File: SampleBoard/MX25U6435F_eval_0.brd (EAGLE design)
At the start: 29.2 x 42.9 mm, 12 parts, among them CN1 MX25U_IF_6PIN, U1 MIC5366-1.8YC5_, U6 MX25U6435F, U7 FXMA108_

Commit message: [WIP] デザイン修正
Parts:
- moved C42 22.9 mm to (7.62, 24.1), flipped to the bottom, turned to 90 degrees
- moved R25 19.9 mm to (2.54, 3.81), flipped to the bottom
- moved C45 15.5 mm to (6.35, 30.5), flipped to the bottom, turned to 270 degrees
- moved C46 12.8 mm to (6.35, 35.6), flipped to the bottom, turned to 90 degrees
- moved U7 10.9 mm to (7.62, 20.3)
- moved U6 10.2 mm to (7.62, 11.4)
- moved U1 9.16 mm to (7.62, 3.81), turned to 90 degrees
- moved C43 5.68 mm to (11.4, 3.81), flipped to the bottom, turned to 270 degrees
- moved C23 4.58 mm to (6.35, 3.81), flipped to the bottom, turned to 270 degrees
- moved R5 4.02 mm to (19.1, 33.0), flipped to the bottom
- moved C24 1.80 mm to (2.54, 24.1), flipped to the bottom
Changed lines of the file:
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@@
 <wire x1="29.19" y1="42.85" x2="0" y2="42.85" width="0" layer="20"/>
 <wire x1="0" y1="42.85" x2="0" y2="0" width="0" layer="20"/>
+<wire x1="0" y1="24.13" x2="12.7" y2="24.13" width="0.4064" layer="51"/>
+<wire x1="12.7" y1="24.13" x2="12.7" y2="0" width="0.4064" layer="51"/>
+<wire x1="12.7" y1="0" x2="0" y2="0" width="0.4064" layer="51"/>
+<wire x1="0" y1="0" x2="0" y2="24.13" width="0.4064" layer="51"/>
 </plain>
 <attributes>
@@
 </autorouter>
 <elements>
-<element name="C23" library="Parts" package="SMD_1608_DEV" value="1uF X5R" x="2.54" y="6.35"/>
-<element name="C24" library="Parts" package="C1210_TPST_DEV" value="10uF" x="3.81" y="25.4" rot="R90"/>
-<element name="C42" library="Parts" package="SMD_1608_DEV" value="0.1uF" x="26.67" y="36.83"/>
-<element name="C43" library="Parts" package="SMD_1608_DEV" value="1uF X5R" x="16.51" y="6.35"/>
-<element name="C45" library="Parts" package="SMD_1608_DEV" value="0.1uF" x="21.59" y="33.02"/>
-<element name="C46" library="Parts" package="SMD_1608_DEV" value="0.1uF" x="19.05" y="36.83"/>
+<element name="C23" library="Parts" package="SMD_1608_DEV" value="1uF X5R" x="6.35" y="3.81" rot="MR270"/>
+<element name="C24" library="Parts" package="C1210_TPST_DEV" value="10uF" x="2.54" y="24.13" rot="MR90"/>
+<element name="C42" library="Parts" package="SMD_1608_DEV" value="0.1uF" x="7.62" y="24.13" rot="MR90"/>
+<element name="C43" library="Parts" package="SMD_1608_DEV" value="1uF X5R" x="11.43" y="3.81" rot="MR270"/>
+<element name="C45" library="Parts" package="SMD_1608_DEV" value="0.1uF" x="6.35" y="30.48" rot="MR270"/>
+<element name="C46" library="Parts" package="SMD_1608_DEV" value="0.1uF" x="6.35" y="35.56" rot="MR90"/>
 <element name="CN1" library="PartsForProto" package="HEADER_6PIN" value="MX25U_IF_6PIN" x="24.13" y="27.94" rot="R270"/>
-<element name="R25" library="Parts" package="SMD_1608_DEV" value="0" x="20.32" y="12.7" rot="R90"/>
-<element name="R5" library="Parts" package="SMD_1608_DEV" value="10k" x="17.78" y="29.21" rot="R90"/>
-<element name="U1" library="Parts" package="SC-70-5_DEV" value="MIC5366-1.8YC5_" x="12.7" y="11.43"/>
-<element name="U6" library="Parts" package="SO8" value="MX25U6435F" x="12.7" y="20.32"/>
-<element name="U7" library="Parts" package="DQFN20_DEV" value="FXMA108_" x="11.43" y="30.48"/>
+<element name="R25" library="Parts" package="SMD_1608_DEV" value="0" x="2.54" y="3.81" rot="MR90"/>
+<element name="R5" library="Parts" package="SMD_1608_DEV" value="10k" x="19.05" y="33.02" rot="MR90"/>
+<element name="U1" library="Parts" package="SC-70-5_DEV" value="MIC5366-1.8YC5_" x="7.62" y="3.81" rot="R90"/>
+<element name="U6" library="Parts" package="SO8" value="MX25U6435F" x="7.62" y="11.43"/>
+<element name="U7" library="Parts" package="DQFN20_DEV" value="FXMA108_" x="7.62" y="20.32"/>
 </elements>
 <signals>
@@
 <contactref element="R25" pad="1"/>
 <contactref element="CN1" pad="1"/>
-<wire x1="20.32" y1="11.6" x2="24.13" y2="27.94" width="0" layer="19" extent="1-1"/>
+<wire x1="2.54" y1="2.71" x2="24.13" y2="27.94" width="0" layer="19" extent="16-16"/>
 </signal>
 <signal name="0V">
@@
 <vertex x="-1.27" y="-1.27"/>
 </polygon>
-<wire x1="22.69" y1="33.02" x2="27.77" y2="36.83" width="0" layer="19" extent="1-1"/>
-<wire x1="20.15" y1="36.83" x2="22.69" y2="33.02" width="0" layer="19" extent="1-1"/>
-<wire x1="17.78" y1="28.11" x2="22.69" y2="33.02" width="0" layer="19" extent="1-1"/>
-<wire x1="14.13" y1="30.23" x2="17.78" y2="28.11" width="0" layer="19" extent="1-1"/>
-<wire x1="3.81" y1="27.1" x2="14.13" y2="30.23" width="0" layer="19" extent="1-1"/>
-<wire x1="14.605" y1="17.72" x2="17.78" y2="28.11" width="0" layer="19" extent="1-1"/>
-<wire x1="12.7" y1="10.005" x2="14.605" y2="17.72" width="0" layer="19" extent="1-1"/>
-<wire x1="17.61" y1="6.35" x2="12.7" y2="10.005" width="0" layer="19" extent="1-1"/>
-<wire x1="3.64" y1="6.35" x2="12.7" y2="10.005" width="0" layer="19" extent="1-1"/>
-<wire x1="24.13" y1="15.24" x2="14.605" y2="17.72" width="0" layer="19" extent="1-1"/>
+<via x="17.78" y="11.43" extent="1-16" drill="0.6"/>
+<via x="16.51" y="20.32" extent="1-16" drill="0.6"/>
+<via x="16.51" y="30.48" extent="1-16" drill="0.6"/>
+<wire x1="16.51" y1="30.48" x2="10.32" y2="20.07" width="0" layer="19" extent="1-1"/>
+<wire x1="9.525" y1="8.83" x2="16.51" y2="20.32" width="0" layer="19" extent="1-1"/>
+<wire x1="9.045" y1="3.81" x2="6.35" y2="2.71" width="0" layer="19" extent="1-16"/>
 </signal>
 <signal name="!CS!">
 <contactref element="U6" pad="1"/>
 <contactref element="U7" pad="3"/>
-<wire x1="10.795" y1="17.72" x2="10.18" y2="28.78" width="0" layer="19" extent="1-1"/>
+<wire x1="5.715" y1="8.83" x2="6.37" y2="18.62" width="0" layer="19" extent="1-1"/>
 </signal>
 <signal name="SI">
 <contactref element="U6" pad="5"/>
 <contactref element="U7" pad="5"/>
-<wire x1="14.605" y1="22.92" x2="11.18" y2="28.78" width="0" layer="19" extent="1-1"/>
+<wire x1="9.525" y1="14.03" x2="7.37" y2="18.62" width="0" layer="19" extent="1-1"/>
 </signal>
 <signal name="SO">
 <contactref element="U6" pad="2"/>
 <contactref element="U7" pad="6"/>
-<wire x1="12.065" y1="17.72" x2="11.68" y2="28.78" width="0" layer="19" extent="1-1"/>
+<wire x1="6.985" y1="8.83" x2="7.87" y2="18.62" width="0" layer="19" extent="1-1"/>
 </signal>
 <signal name="SCLK">
 <contactref element="U6" pad="6"/>
 <contactref element="U7" pad="8"/>
-<wire x1="13.335" y1="22.92" x2="12.68" y2="28.78" width="0" layer="19" extent="1-1"/>
+<wire x1="8.255" y1="14.03" x2="8.87" y2="18.62" width="0" layer="19" extent="1-1"/>
 </signal>
 <signal name="VCC_MEM">
@@
 <contactref element="U7" pad="20"/>
 <contactref element="C46" pad="1"/>
-<wire x1="8.73" y1="30.73" x2="17.95" y2="36.83" width="0" layer="19" extent="1-1"/>
-<wire x1="20.32" y1="13.8" x2="8.73" y2="30.73" width="0" layer="19" extent="1-1"/>
-<wire x1="13.35" y1="10.005" x2="20.32" y2="13.8" width="0" layer="19" extent="1-1"/>
-<wire x1="12.05" y1="10.005" x2="13.35" y2="10.005" width="0" layer="19" extent="1-1"/>
-<wire x1="15.41" y1="6.35" x2="13.35" y2="10.005" width="0" layer="19" extent="1-1"/>
+<wire x1="6.35" y1="34.46" x2="4.92" y2="20.57" width="0" layer="19" extent="1-16"/>
+<wire x1="9.045" y1="4.46" x2="4.92" y2="20.57" width="0" layer="19" extent="1-1"/>
+<wire x1="9.045" y1="3.16" x2="9.045" y2="4.46" width="0" layer="19" extent="1-1"/>
+<wire x1="11.43" y1="4.91" x2="9.045" y2="3.16" width="0" layer="19" extent="1-16"/>
+<wire x1="2.54" y1="4.91" x2="9.045" y2="3.16" width="0" layer="19" extent="1-16"/>
 </signal>
 <signal name="!OE!">
 <contactref element="R5" pad="2"/>
 <contactref element="U7" pad="11"/>
-<wire x1="14.13" y1="30.73" x2="17.78" y2="30.31" width="0" layer="19" extent="1-1"/>
+<via x="16.51" y="35.56" extent="1-16" drill="0.6"/>
+<wire x1="16.51" y1="35.56" x2="19.05" y2="34.12" width="0" layer="19" extent="16-16"/>
+<wire x1="10.32" y1="20.57" x2="16.51" y2="35.56" width="0" layer="19" extent="1-1"/>
 </signal>
 <signal name="+1V8">
@@
 <contactref element="U7" pad="1"/>
 <contactref element="C45" pad="1"/>
-<wire x1="20.49" y1="33.02" x2="25.57" y2="36.83" width="0" layer="19" extent="1-1"/>
-<wire x1="8.73" y1="30.23" x2="20.49" y2="33.02" width="0" layer="19" extent="1-1"/>
-<wire x1="10.795" y1="22.92" x2="8.73" y2="30.23" width="0" layer="19" extent="1-1"/>
-<wire x1="12.065" y1="22.92" x2="10.795" y2="22.92" width="0" layer="19" extent="1-1"/>
-<wire x1="13.335" y1="17.72" x2="12.065" y2="22.92" width="0" layer="19" extent="1-1"/>
-<wire x1="12.05" y1="12.855" x2="13.335" y2="17.72" width="0" layer="19" extent="1-1"/>
-<wire x1="3.81" y1="23.7" x2="10.795" y2="22.92" width="0" layer="19" extent="1-1"/>
-<wire x1="1.44" y1="6.35" x2="12.05" y2="12.855" width="0" layer="19" extent="1-1"/>
+<wire x1="6.35" y1="31.58" x2="4.92" y2="20.07" width="0" layer="19" extent="1-16"/>
+<wire x1="7.62" y1="23.03" x2="6.35" y2="31.58" width="0" layer="19" extent="16-16"/>
+<wire x1="5.715" y1="14.03" x2="7.62" y2="23.03" width="0" layer="19" extent="1-16"/>
+<wire x1="6.985" y1="14.03" x2="5.715" y2="14.03" width="0" layer="19" extent="1-1"/>
+<wire x1="2.54" y1="22.43" x2="7.62" y2="23.03" width="0" layer="19" extent="16-16"/>
+<wire x1="8.255" y1="8.83" x2="6.985" y2="14.03" width="0" layer="19" extent="1-1"/>
+<wire x1="6.35" y1="4.91" x2="8.255" y2="8.83" width="0" layer="19" extent="1-16"/>
+<wire x1="6.195" y1="3.16" x2="6.35" y2="4.91" width="0" layer="19" extent="1-16"/>
 </signal>
 <signal name="PA15">
 <contactref element="U7" pad="18"/>
 <contactref element="CN1" pad="2"/>
-<wire x1="10.18" y1="32.18" x2="24.13" y2="25.4" width="0" layer="19" extent="1-1"/>
+<wire x1="6.37" y1="22.02" x2="24.13" y2="25.4" width="0" layer="19" extent="1-1"/>
 </signal>
 <signal name="PC12">
 <contactref element="U7" pad="16"/>
 <contactref element="CN1" pad="3"/>
-<wire x1="11.18" y1="32.18" x2="24.13" y2="22.86" width="0" layer="19" extent="1-1"/>
+<wire x1="7.37" y1="22.02" x2="24.13" y2="22.86" width="0" layer="19" extent="1-1"/>
 </signal>
 <signal name="PC11">
 <contactref element="U7" pad="15"/>
 <contactref element="CN1" pad="4"/>
-<wire x1="11.68" y1="32.18" x2="24.13" y2="20.32" width="0" layer="19" extent="1-1"/>
+<wire x1="24.13" y1="20.32" x2="7.87" y2="22.02" width="0" layer="19" extent="1-1"/>
 </signal>
 <signal name="PC10">
 <contactref element="U7" pad="13"/>
 <contactref element="CN1" pad="5"/>
-<wire x1="24.13" y1="17.78" x2="12.68" y2="32.18" width="0" layer="19" extent="1-1"/>
+<wire x1="24.13" y1="17.78" x2="8.87" y2="22.02" width="0" layer="19" extent="1-1"/>
 </signal>
 </signals>

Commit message: 配線を全面的に修正
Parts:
- moved CN1 22.9 mm to (16.5, 6.35), turned to 90 degrees
- moved C24 16.7 mm to (7.62, 8.26), turned to 180 degrees
- moved C45 16.6 mm to (5.08, 14.0), turned to 180 degrees
- moved R5 13.5 mm to (10.2, 22.9), turned to 180 degrees
- moved R25 13.0 mm to (15.2, 1.27), turned to 0 degrees
- moved C46 12.8 mm to (5.08, 22.9), turned to 180 degrees
- moved C42 6.84 mm to (5.08, 17.8), turned to 180 degrees
- moved C23 4.46 mm to (1.91, 3.49), turned to 90 degrees
- moved C43 3.88 mm to (8.26, 1.59), turned to 0 degrees
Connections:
- net PC10: now also U7.16; no longer U7.13
- net PC11: now also U7.14; no longer U7.15
- net PC12: now also U7.12; no longer U7.16
- net SCLK: now also U7.5; no longer U7.8
- net SI: now also U7.9; no longer U7.5
- net SO: now also U7.7; no longer U7.6
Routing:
- net VCC_MEM: track 0.00 -> 52.0 mm, vias 0 -> 3
- net +1V8: track 0.00 -> 45.3 mm, vias 0 -> 4
- net PA15: track 0.00 -> 28.3 mm
- net PC12: track 0.00 -> 18.3 mm
- net PC11: track 0.00 -> 17.9 mm
- net PC10: track 0.00 -> 17.5 mm
- net !CS!: track 0.00 -> 11.1 mm
- net SO: track 0.00 -> 10.8 mm
- net 0V: track 0.00 -> 8.37 mm
- net +3V3: track 0.00 -> 5.15 mm
- net SCLK: track 0.00 -> 4.96 mm
- net SI: track 0.00 -> 4.65 mm
- net !OE!: track 0.00 -> 4.14 mm
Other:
- board size 29.2 x 42.9 mm -> 19.1 x 25.4 mm

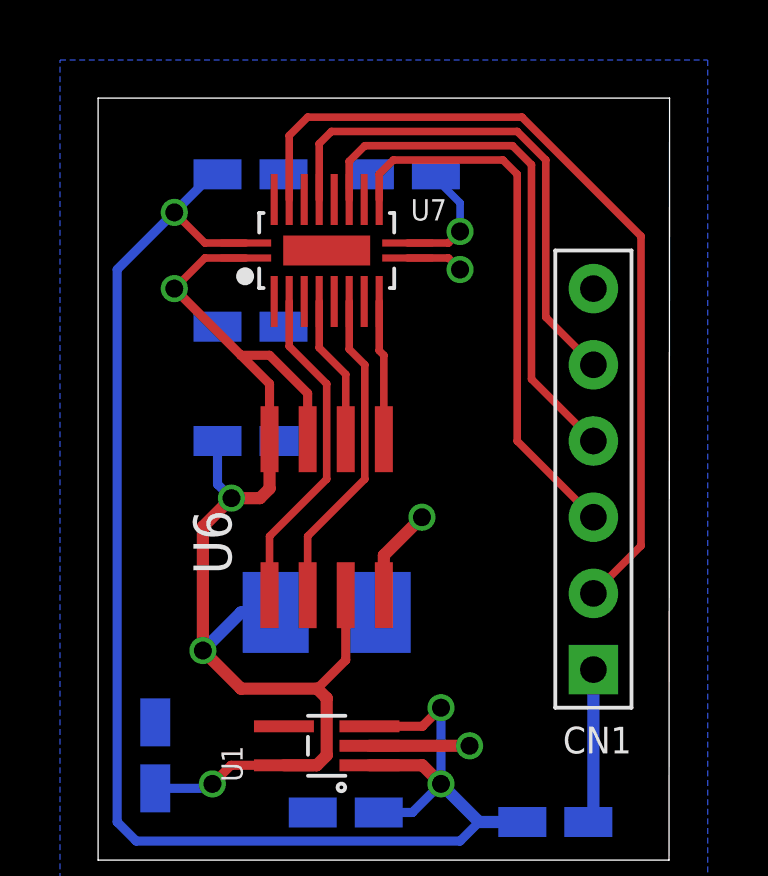
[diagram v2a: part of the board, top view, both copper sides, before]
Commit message: 評価回路を修正
・配線を小修正
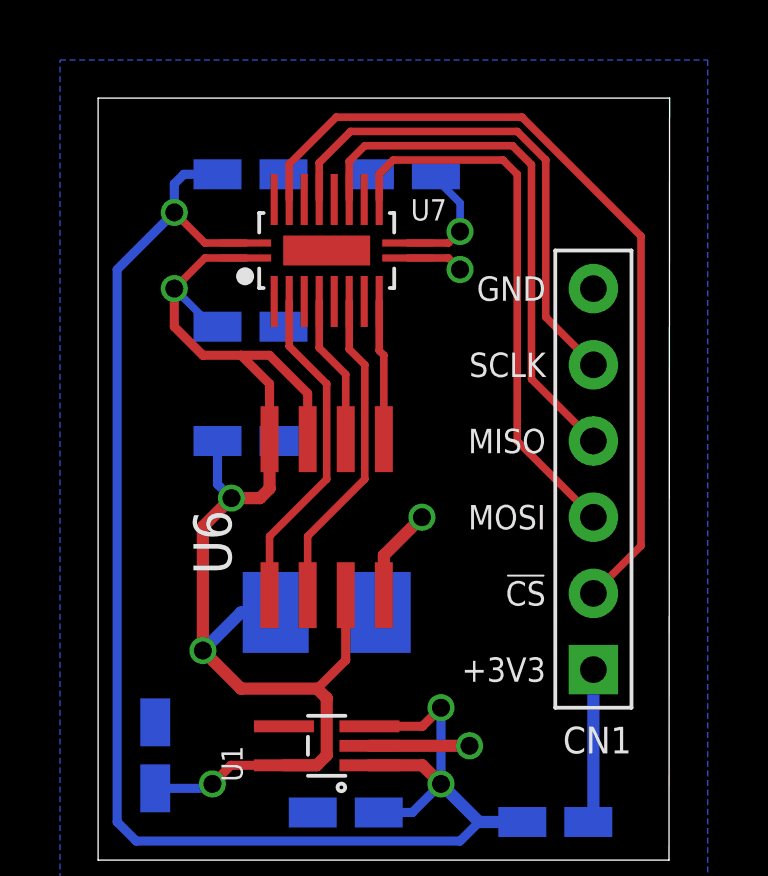
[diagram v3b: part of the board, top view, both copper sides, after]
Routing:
- net +1V8: track 45.3 -> 46.1 mm
- net VCC_MEM: track 52.0 -> 52.6 mm
- net PA15: track 28.3 -> 27.8 mm
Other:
- board text added: "!CS!"
- board text added: "+3V3"
- board text added: "GND"
- board text added: "MISO"
- board text added: "MOSI"
- board text added: "SCLK"
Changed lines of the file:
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@@
 <setting verticaltext="up"/>
 </settings>
-<grid distance="0.05" unitdist="inch" unit="mil" style="lines" multiple="1" display="yes" altdistance="0.025" altunitdist="inch" altunit="inch"/>
+<grid distance="12.5" unitdist="mil" unit="mil" style="lines" multiple="1" display="yes" altdistance="0.025" altunitdist="inch" altunit="inch"/>
 <layers>
 <layer number="1" name="Top" color="4" fill="1" visible="yes" active="yes"/>
@@
 <wire x1="19.05" y1="25.4" x2="0" y2="25.4" width="0" layer="20"/>
 <wire x1="0" y1="25.4" x2="0" y2="0" width="0" layer="20"/>
+<text x="14.9225" y="19.05" size="0.8128" layer="21" align="center-right">GND</text>
+<text x="14.9225" y="16.51" size="0.8128" layer="21" align="center-right">SCLK</text>
+<text x="14.9225" y="13.97" size="0.8128" layer="21" align="center-right">MISO</text>
+<text x="14.9225" y="11.43" size="0.8128" layer="21" align="center-right">MOSI</text>
+<text x="14.9225" y="8.89" size="0.8128" layer="21" align="center-right">!CS!</text>
+<text x="14.9225" y="6.35" size="0.8128" layer="21" align="center-right">+3V3</text>
 </plain>
 <attributes>
@@
 <wire x1="4.92" y1="20.57" x2="3.56" y2="20.57" width="0.254" layer="1"/>
 <wire x1="3.56" y1="20.57" x2="2.54" y2="21.59" width="0.254" layer="1"/>
-<wire x1="2.54" y1="21.59" x2="3.81" y2="22.86" width="0.3048" layer="16"/>
-<wire x1="3.81" y1="22.86" x2="3.98" y2="22.86" width="0.3048" layer="16"/>
 <wire x1="12.7" y1="1.27" x2="12.065" y2="0.635" width="0.3048" layer="16"/>
 <wire x1="12.065" y1="0.635" x2="1.27" y2="0.635" width="0.3048" layer="16"/>
@@
 <wire x1="11.43" y1="2.54" x2="12.7" y2="1.27" width="0.4064" layer="16"/>
 <wire x1="14.14" y1="1.27" x2="12.7" y2="1.27" width="0.4064" layer="16"/>
+<wire x1="3.98" y1="22.86" x2="2.8575" y2="22.86" width="0.3048" layer="16"/>
+<wire x1="2.8575" y1="22.86" x2="2.54" y2="22.5425" width="0.3048" layer="16"/>
+<wire x1="2.54" y1="22.5425" x2="2.54" y2="21.59" width="0.3048" layer="16"/>
 </signal>
 <signal name="!OE!">
@@
 <wire x1="5.715" y1="14.03" x2="5.715" y2="15.875" width="0.3048" layer="1"/>
 <wire x1="5.715" y1="15.875" x2="4.7625" y2="16.8275" width="0.3048" layer="1"/>
-<wire x1="4.7625" y1="16.8275" x2="2.54" y2="19.05" width="0.3048" layer="1"/>
 <wire x1="6.985" y1="14.03" x2="6.985" y2="15.5575" width="0.3048" layer="1"/>
 <wire x1="3.98" y1="13.97" x2="3.98" y2="12.53" width="0.3048" layer="16"/>
@@
 <wire x1="8.255" y1="8.83" x2="8.255" y2="6.6675" width="0.3048" layer="1"/>
 <wire x1="8.255" y1="6.6675" x2="7.3025" y2="5.715" width="0.3048" layer="1"/>
+<wire x1="4.7625" y1="16.8275" x2="3.4925" y2="16.8275" width="0.3048" layer="1"/>
+<wire x1="3.4925" y1="16.8275" x2="2.54" y2="17.78" width="0.3048" layer="1"/>
+<wire x1="2.54" y1="17.78" x2="2.54" y2="19.05" width="0.3048" layer="1"/>
 </signal>
 <signal name="PA15">
 <contactref element="U7" pad="18"/>
 <contactref element="CN1" pad="2"/>
-<wire x1="6.37" y1="22.02" x2="6.37" y2="24.15" width="0.254" layer="1"/>
-<wire x1="6.37" y1="24.15" x2="6.985" y2="24.765" width="0.254" layer="1"/>
 <wire x1="18.0975" y1="10.4775" x2="16.51" y2="8.89" width="0.254" layer="1"/>
-<wire x1="6.985" y1="24.765" x2="14.12875" y2="24.765" width="0.254" layer="1"/>
+<wire x1="7.9375" y1="24.765" x2="14.12875" y2="24.765" width="0.254" layer="1"/>
 <wire x1="14.12875" y1="24.765" x2="18.0975" y2="20.79625" width="0.254" layer="1"/>
 <wire x1="18.0975" y1="20.79625" x2="18.0975" y2="10.4775" width="0.254" layer="1"/>
+<wire x1="6.37" y1="22.02" x2="6.37" y2="23.1975" width="0.254" layer="1"/>
+<wire x1="6.37" y1="23.1975" x2="7.9375" y2="24.765" width="0.254" layer="1"/>
 </signal>
 <signal name="PC12">
@@
 <contactref element="CN1" pad="5"/>
 <contactref element="U7" pad="16"/>
-<wire x1="7.37" y1="22.02" x2="7.37" y2="23.88" width="0.254" layer="1"/>
-<wire x1="7.37" y1="23.88" x2="7.77875" y2="24.28875" width="0.254" layer="1"/>
 <wire x1="14.9225" y1="18.0975" x2="16.51" y2="16.51" width="0.254" layer="1"/>
-<wire x1="7.77875" y1="24.28875" x2="13.97" y2="24.28875" width="0.254" layer="1"/>
+<wire x1="8.41375" y1="24.28875" x2="13.97" y2="24.28875" width="0.254" layer="1"/>
 <wire x1="13.97" y1="24.28875" x2="14.9225" y2="23.33625" width="0.254" layer="1"/>
 <wire x1="14.9225" y1="23.33625" x2="14.9225" y2="18.0975" width="0.254" layer="1"/>
+<wire x1="7.37" y1="22.02" x2="7.37" y2="23.245" width="0.254" layer="1"/>
+<wire x1="7.37" y1="23.245" x2="8.41375" y2="24.28875" width="0.254" layer="1"/>
 </signal>
 </signals>
